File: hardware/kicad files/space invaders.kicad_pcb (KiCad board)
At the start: 2 copper layers, 94.8 x 95.9 mm, 36 parts, among them J1 ICSP, J2 RE, J3 RD, J4 RC5/6/7, J5 RC0/1/2, J6 RA6/7, J7 Conn_01x04_Pin, J8 RB1/2/3/4/5, J9 USB_C_Receptacle_PowerOnly_6P, SW1 RESET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

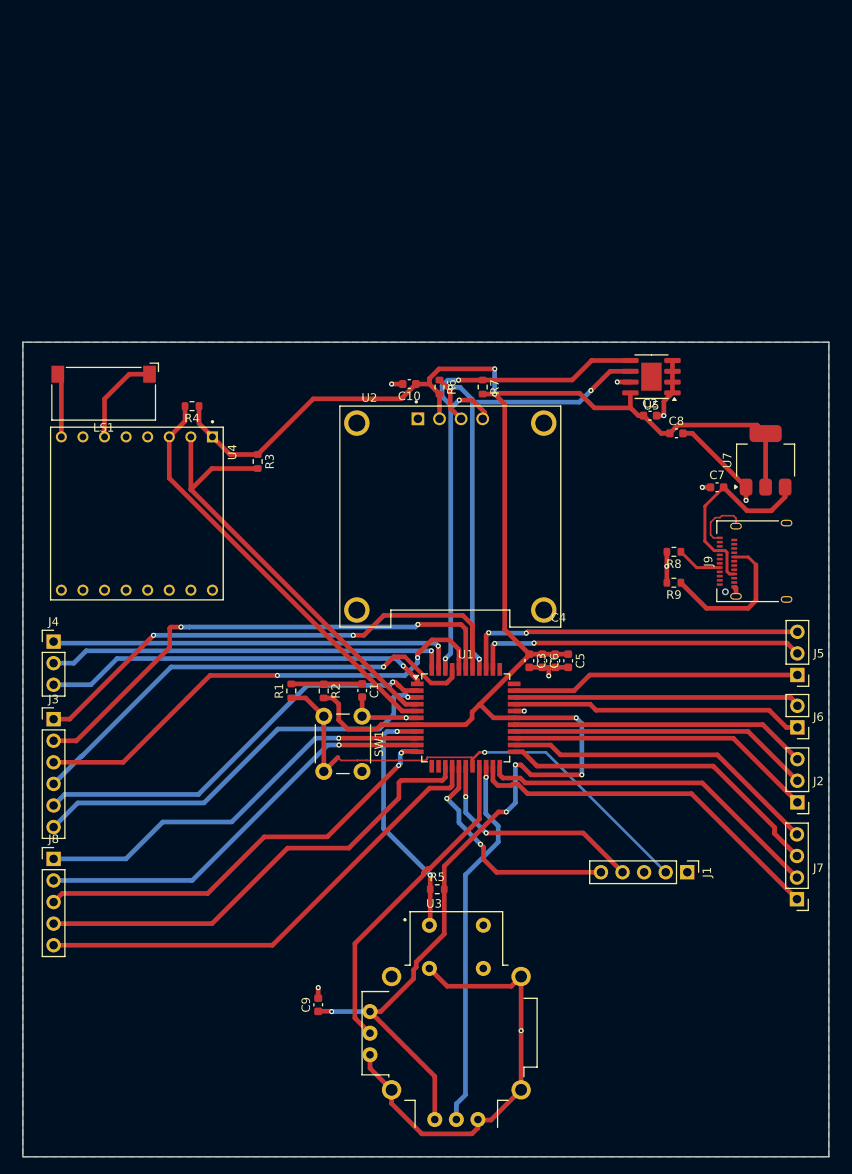
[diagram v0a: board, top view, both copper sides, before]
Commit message: Added Serial to PCB
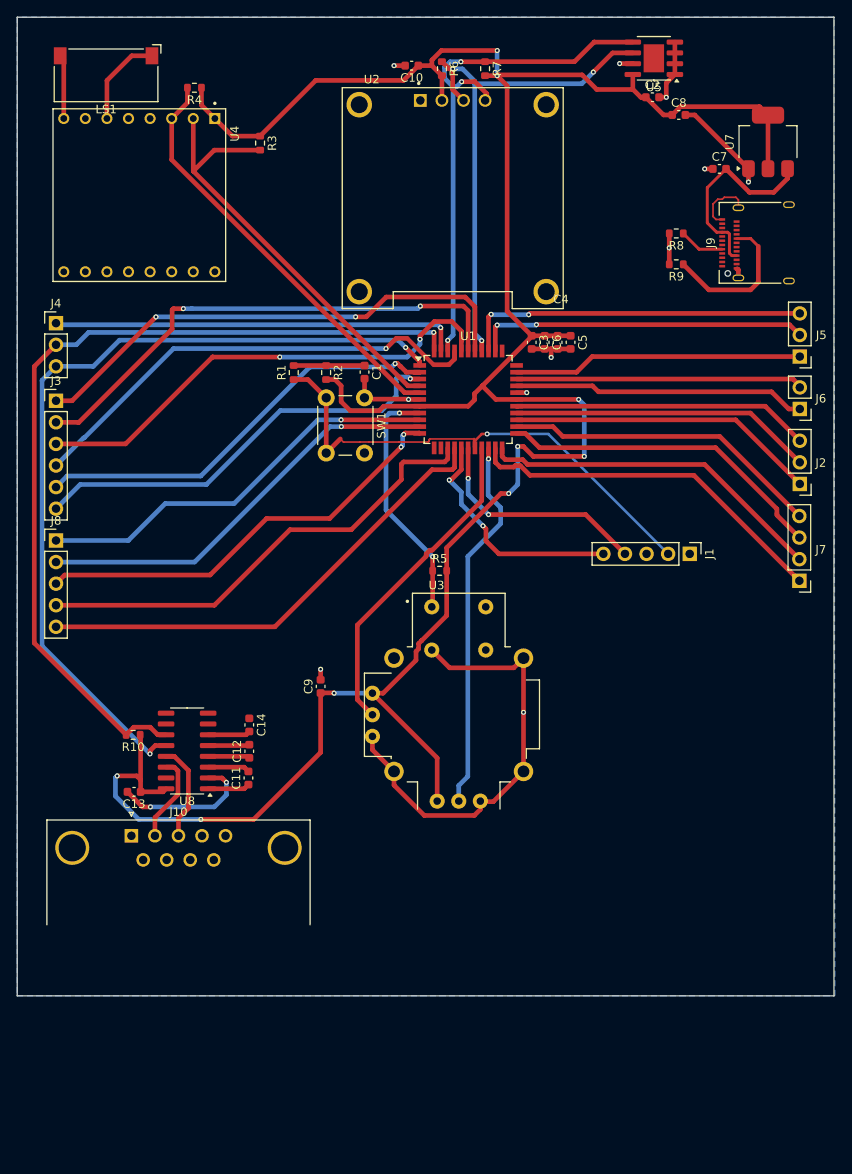
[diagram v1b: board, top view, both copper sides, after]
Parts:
- added C11: 1uF, Capacitor_SMD:C_0603_1608Metric, F.Cu at (129.2, 111.2)
- added C12: 1uF, Capacitor_SMD:C_0603_1608Metric, F.Cu at (129.3, 108.1)
- added C13: 1uF, Capacitor_SMD:C_0603_1608Metric, F.Cu at (115.8, 112.8)
- added C14: 1uF, Capacitor_SMD:C_0603_1608Metric, F.Cu at (129.3, 105.0)
- added J10: DE9_Socket, Connector_Dsub:DSUB-9_Pins_Horizontal_P2.77x2.84mm_EdgePinOffset7.70mm_Housed_MountingHolesOffset9.12mm, F.Cu at (115.4, 118.0)
- added R10: 10k, Resistor_SMD:R_0603_1608Metric, F.Cu at (115.7, 106.1)
- added U8: MAX3232CDR, Package_SO:SOIC-16_3.9x9.9mm_P1.27mm, F.Cu at (122.0, 108.0)
- moved C7 37.5 mm to (184.6, 39.5)
- moved R8 37.5 mm to (179.6, 47.1)
- moved U2 37.5 mm to (153.3, 43.0)
- moved C10 37.5 mm to (148.4, 27.4)
- moved C2 37.5 mm to (176.8, 31.1)
- moved C9 37.5 mm to (137.7, 100.4)
- moved J2 37.5 mm to (194.1, 76.6)
- moved J3 37.5 mm to (106.6, 66.8)
- moved J5 37.5 mm to (194.1, 61.6)
- moved J7 37.5 mm to (194.0, 88.0)
- moved J8 37.5 mm to (106.6, 83.3)
- moved LS1 37.5 mm to (112.5, 28.5)
- moved R3 37.5 mm to (130.6, 36.5)
- moved R4 37.5 mm to (122.9, 30.0)
- moved R5 37.5 mm to (151.7, 86.8)
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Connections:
- net Net-(J4-Pin_2) renamed Tx1
- net Net-(J4-Pin_3) renamed Rx1
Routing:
- net Tx1: track 47.3 -> 104.1 mm
- net Rx1: track 45.6 -> 99.6 mm, vias 1 -> 2
- net VDD: track 246.8 -> 297.7 mm, vias 7 -> 9
- net Net-(U8-V+): track 0.00 -> 16.8 mm, vias 0 -> 2
- net RXD: track 0.00 -> 11.5 mm
- net Net-(U8-DOUT1): track 0.00 -> 10.4 mm
- net Net-(U8-V-): track 0.00 -> 5.00 mm
- net Net-(U8-C1-): track 0.00 -> 4.95 mm
- net Net-(U8-C1+): track 0.00 -> 4.94 mm
- net Net-(U8-C2+): track 0.00 -> 4.91 mm
- net Net-(U8-C2-): track 0.00 -> 4.88 mm
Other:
- board size 94.8 x 95.9 mm -> 96.1 x 115.2 mm
